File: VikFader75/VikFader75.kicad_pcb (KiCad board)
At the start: 2 copper layers, 75.6 x 9 mm, 17 parts, among them J1 vik-module-connector, J3 Conn_01x04_Pin, U1 ADS1015IDGS

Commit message: Various DRC fixes
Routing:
- net GND: track 11.9 -> 19.6 mm
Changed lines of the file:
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@@
 		)
+	)
+	(segment
+		(start 136.85 96.85)
+		(end 135.32 96.85)
+		(width 0.2)
+		(layer "F.Cu")
+		(net 1)
+	)
+	(segment
+		(start 139.4 94.3)
+		(end 136.85 96.85)
+		(width 0.2)
+		(layer "F.Cu")
+		(net 1)
+	)
+	(segment
+		(start 138.08 92.98)
+		(end 138.08 92.309)
+		(width 0.2)
+		(layer "F.Cu")
+		(net 1)
+	)
+	(segment
+		(start 139.4 94.3)
+		(end 138.08 92.98)
+		(width 0.2)
+		(layer "F.Cu")
+		(net 1)
 	)
 	(via

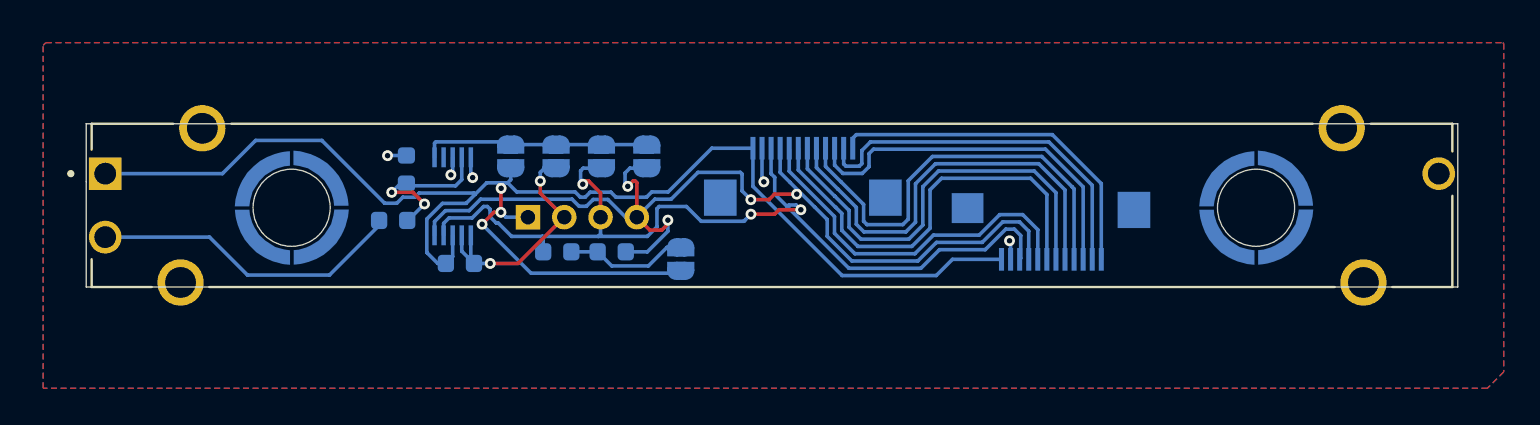
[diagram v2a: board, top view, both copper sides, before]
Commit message: Updated 75 to new MOSFET design
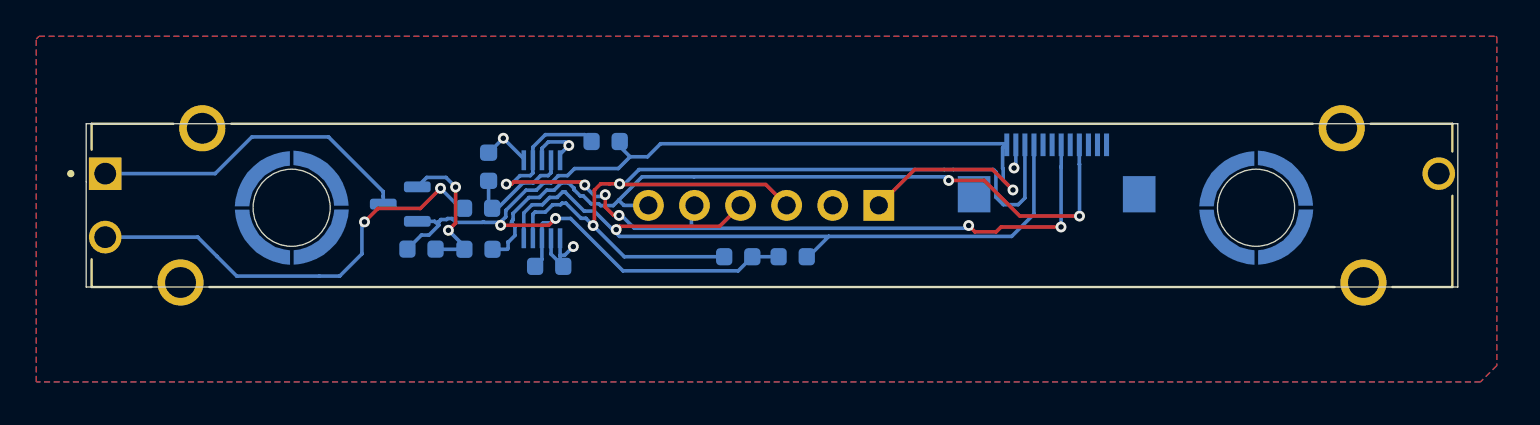
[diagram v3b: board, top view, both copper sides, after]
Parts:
- removed J3: Conn_01x04_Pin, Connector_PinHeader_2.00mm:PinHeader_1x04_P2.00mm_Vertical
- removed JP1: 0x48, Jumper:SolderJumper-2_P1.3mm_Open_RoundedPad1.0x1.5mm
- removed JP2: 0x49, Jumper:SolderJumper-2_P1.3mm_Open_RoundedPad1.0x1.5mm
- removed JP3: 0x4A, Jumper:SolderJumper-2_P1.3mm_Open_RoundedPad1.0x1.5mm
- removed JP4: 0x4B, Jumper:SolderJumper-2_P1.3mm_Open_RoundedPad1.0x1.5mm
- removed JP5: Jumper_2_Small_Open, Jumper:SolderJumper-2_P1.3mm_Open_RoundedPad1.0x1.5mm
- added Q1: DMG2305UX, Package_TO_SOT_SMD:SOT-23, B.Cu at (130.4, 93.6)
- added R5: 1kΩ, Capacitor_SMD:C_0603_1608Metric, B.Cu at (134.7, 96.1)
- added R6: 100kΩ, Capacitor_SMD:C_0603_1608Metric, B.Cu at (131.5, 96.1)
- added R7: 10kΩ, Capacitor_SMD:C_0603_1608Metric, B.Cu at (141.7, 90.1)
- J2: value ~ -> Conn_01x06_Pin; footprint vik-fader:vik-keyboard-connector-horizontal -> Connector_PinHeader_2.54mm:PinHeader_1x06_P2.54mm_Vertical
- U1: value ADS1015IDGS -> ADS1115IDGS
- moved J1 14.0 mm to (166.5, 92.3)
- moved R2 9.98 mm to (149.0, 96.5)
- moved R3 9.98 mm to (152.0, 96.5)
- moved J2 9.56 mm to (156.7, 93.7), turned to 90 degrees
- moved C2 4.92 mm to (138.6, 97.0)
- moved U1 4.92 mm to (138.2, 93.3)
- moved R4 4.73 mm to (134.7, 93.8)
- moved C1 4.53 mm to (135.2, 91.5)
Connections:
- J2 pad 5: RGB -> GP1
- J2 pad 6: 5v -> GP2
- R1 pad 1: +3V3 -> FET-OUT
- R2 pad 1: Net-(JP5-A) -> +3V3
- R3 pad 1: Net-(JP5-A) -> +3V3
- U1 pad 1: Net-(JP1-A) -> GND
- U1 pad 2: unconnected-(U1-ALERT/RDY-Pad2) -> GP1
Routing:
- net MOSI: track 24.0 -> 0.00 mm
- net 5v: track 23.9 -> 0.00 mm
- net GP1: track 24.0 -> 45.2 mm, vias 0 -> 6
- net MISO: track 20.7 -> 0.00 mm
- net CS: track 20.7 -> 0.00 mm
- net RGB: track 20.3 -> 0.00 mm
- net SCLK: track 19.6 -> 0.00 mm
- net GP2: track 24.0 -> 42.8 mm, vias 0 -> 2
- net FET-OUT: track 0.00 -> 18.1 mm
- net +3V3: track 84.4 -> 70.5 mm
- net Net-(JP1-A): track 12.6 -> 0.00 mm
- net SCL: track 55.0 -> 44.5 mm, vias 4 -> 1
- net Net-(Q1-G): track 0.00 -> 8.43 mm, vias 0 -> 2
- net GND: track 19.6 -> 11.9 mm, vias 7 -> 4
- net Net-(JP5-A): track 6.78 -> 0.00 mm
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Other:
- board text added: "FET"
- board text added: "RDY"
- board text removed: "0x48"
- board text removed: "0x49"
- board text removed: "0x4A"
- board text removed: "0x4B"
- board text removed: "I2C -> PULL UP"

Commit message: All three models refactored to MOSFET setup
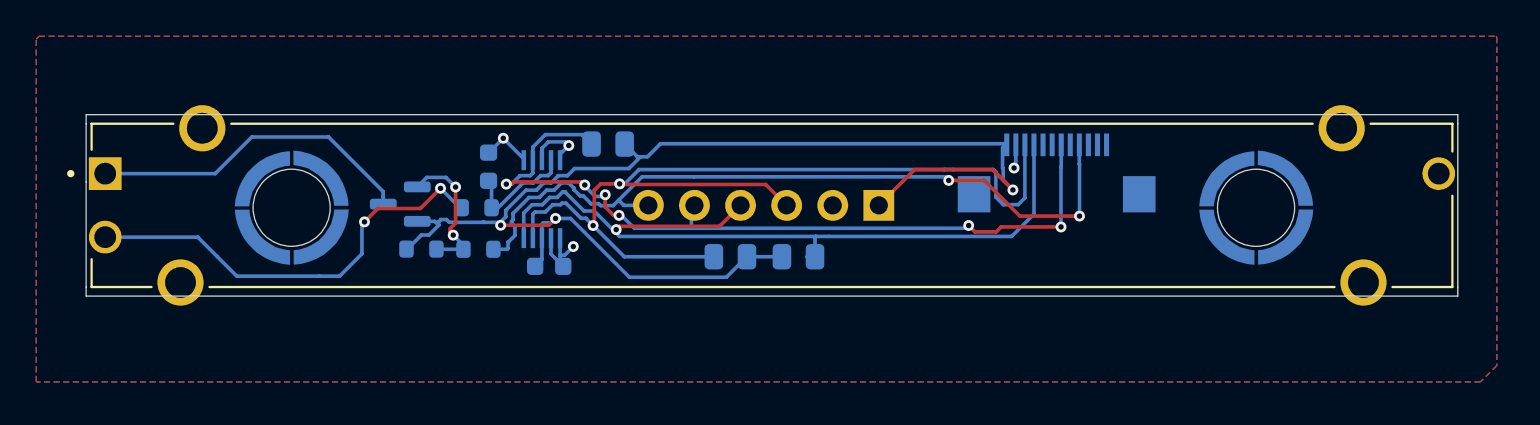
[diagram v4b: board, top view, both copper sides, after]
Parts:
- R2, R3, R7: footprint Capacitor_SMD:C_0603_1608Metric -> Resistor_SMD:R_0805_2012Metric
- R4, R5, R6: footprint Capacitor_SMD:C_0603_1608Metric -> Resistor_SMD:R_0603_1608Metric
- moved R2 0.43 mm to (148.6, 96.5)
- moved R3 0.32 mm to (152.3, 96.5)
- moved R7 0.20 mm to (141.8, 90.3)
- moved R4 0.09 mm to (134.6, 93.8)
- turned R5 to 0 degrees
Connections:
- R5 pad 1: GP2 -> Net-(Q1-G)
- R5 pad 2: Net-(Q1-G) -> GP2
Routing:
- net SDA: track 54.1 -> 53.5 mm
- net +3V3: track 70.5 -> 71.0 mm
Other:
- board size 75.6 x 9 mm -> 75.6 x 10 mm
